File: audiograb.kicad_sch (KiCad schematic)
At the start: 6 parts, among them J1 USB_C_Receptacle_USB2.0_16P, U12 IP4220CZ6F

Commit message: earth plane, vias, connector ect
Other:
- added sheet div (div.kicad_sch)
- note removed: "bytta navn for å unngaa label konflikt"
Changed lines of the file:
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@@
-		)
-	)
-	(text "bytta navn for å\nunngaa label konflikt"
-		(exclude_from_sim no)
-		(at 256.794 66.548 0)
-		(effects
-			(font
-				(size 1.27 1.27)
-			)
 		)
 	)
@@
 				)
 			)
+		)
+	)
+	(sheet
+		(at 217.424 122.174)
+		(size 36.576 22.352)
+		(exclude_from_sim no)
+		(in_bom yes)
+		(on_board yes)
+		(dnp no)
+		(fields_autoplaced yes)
+		(stroke
+			(width 0.1524)
+			(type solid)
+		)
+		(fill
+			(color 0 0 0 0.0000)
+		)
+		(property "Sheetname" "div"
+			(at 217.424 121.4624 0)
+			(effects
+				(font
+					(size 1.27 1.27)
+				)
+				(justify left bottom)
+			)
+		)
+		(property "Sheetfile" "div.kicad_sch"
+			(at 217.424 145.1106 0)
+			(effects
+				(font
+					(size 1.27 1.27)
+				)
+				(justify left top)
+			)
+		)
+		(instances
+			(project "audiograb"
+				(path "/c46c2311-6d4b-411d-b012-c7730eac136d"
+					(page "6")
+				)
+			)

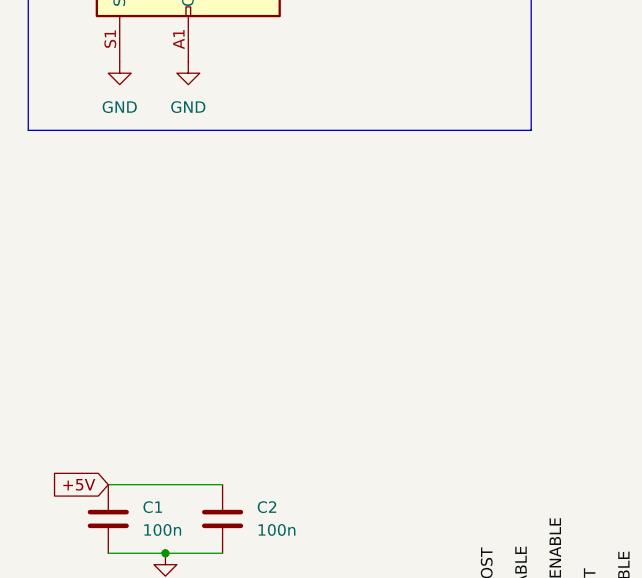
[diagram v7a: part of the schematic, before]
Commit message: add connector for BMS to schematic
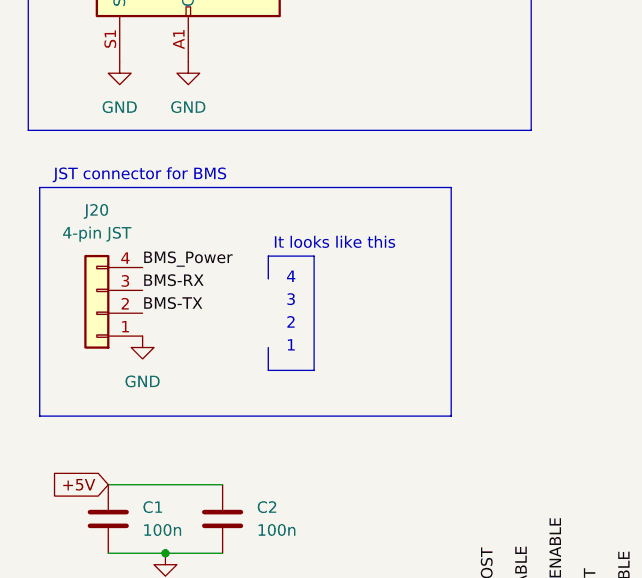
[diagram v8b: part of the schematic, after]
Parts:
- added J20: 4-pin JST, 4ms_Connector:Pins_1x04_2.54mm_TH_SWD, symbol PCM_4ms_Connector:Conn_01x04
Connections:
- net GND: now also J20.1 (Pin_1)
- new net BMS-RX: J20.3 (Pin_3)
- new net BMS-TX: J20.2 (Pin_2)
- new net BMS_Power: J20.4 (Pin_4)
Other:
- note added: "1"
- note added: "2"
- note added: "3"
- note added: "4"
- note added: "It looks like this"
- note added: "JST connector for BMS"
